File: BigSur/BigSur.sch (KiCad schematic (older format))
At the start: 0 parts

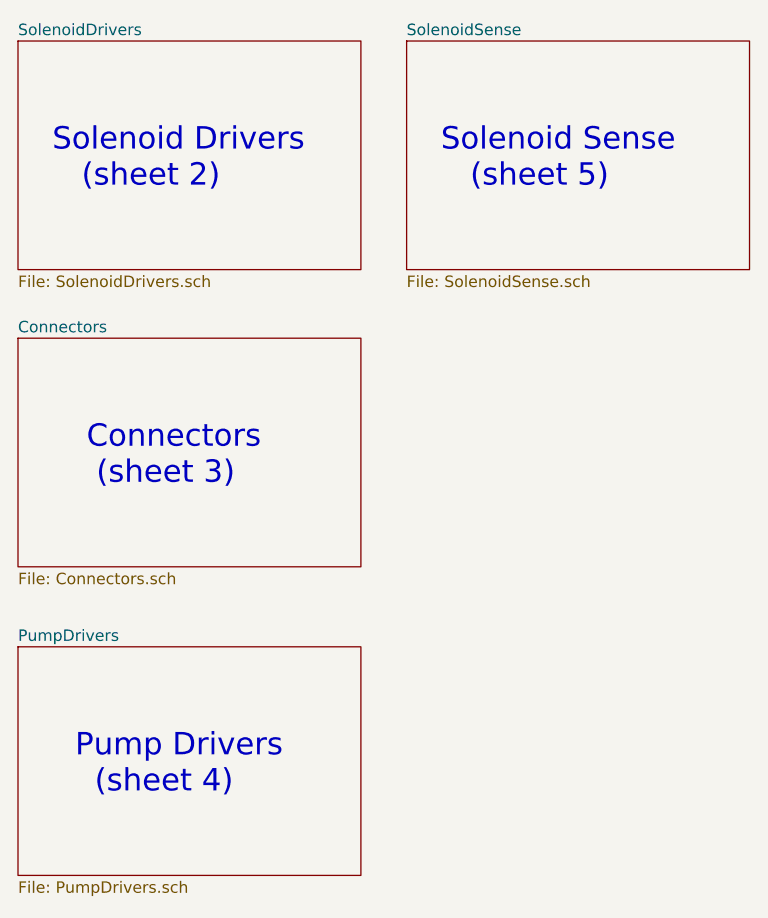
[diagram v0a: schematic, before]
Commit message: Added mounting holes, CAN connector,  indicator LEDs, started general purpose relays
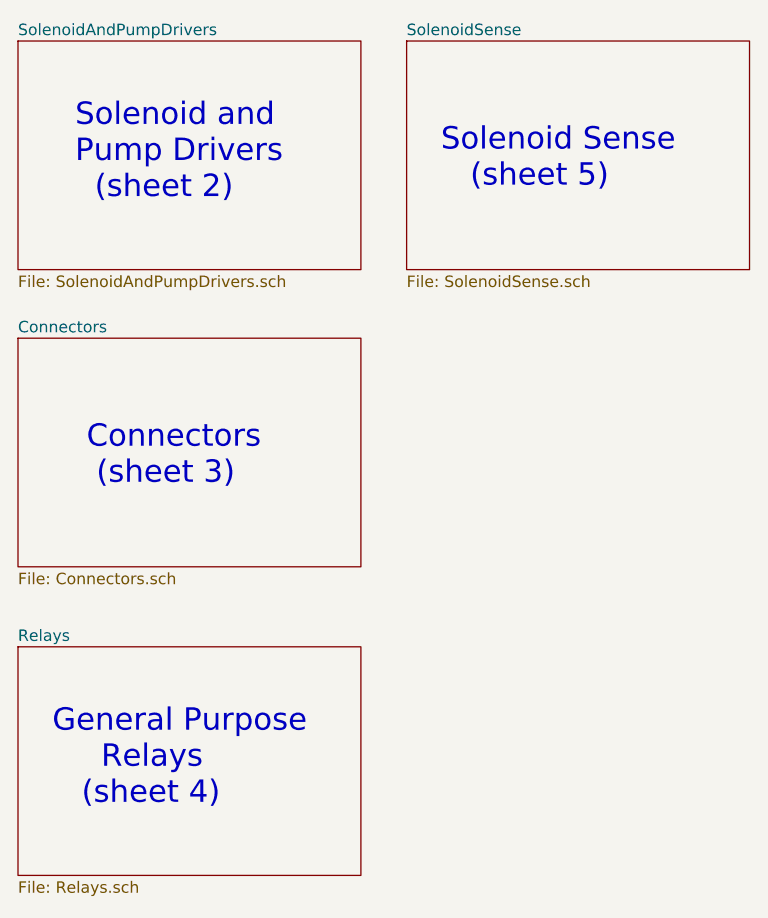
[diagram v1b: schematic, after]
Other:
- note added: "General Purpose\n Relays\n (sheet 4)"
- note added: "Solenoid and\nPump Drivers\n (sheet 2)"
- note removed: "Pump Drivers\n (sheet 4)"
- note removed: "Solenoid Drivers\n (sheet 2)"
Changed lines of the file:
@@
 EESchema Schematic File Version 4
 LIBS:BigSur-cache
-EELAYER 29 0
+EELAYER 30 0
 EELAYER END
 $Descr A4 11693 8268
@@
 S 1950 1450 1500 1000
 U 5D6EB2B2
-F0 "SolenoidDrivers" 50
-F1 "SolenoidDrivers.sch" 50
+F0 "SolenoidAndPumpDrivers" 50
+F1 "SolenoidAndPumpDrivers.sch" 50
 $EndSheet
 $Sheet
@@
 S 1950 4100 1500 1000
 U 5D7D29A6
-F0 "PumpDrivers" 50
-F1 "PumpDrivers.sch" 50
+F0 "Relays" 50
+F1 "Relays.sch" 50
 $EndSheet
-Text Notes 2200 4750 0    98   ~ 0
-Pump Drivers\n  (sheet 4)
-Text Notes 2100 2100 0    98   ~ 0
-Solenoid Drivers\n   (sheet 2)
+Text Notes 2100 4800 0    98   ~ 0
+General Purpose\n     Relays\n   (sheet 4)
+Text Notes 2200 2150 0    98   ~ 0
+Solenoid and\nPump Drivers\n  (sheet 2)
 $Sheet
 S 3650 1450 1500 1000
